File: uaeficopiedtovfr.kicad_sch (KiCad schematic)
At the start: 35 parts, among them J1 USB_B_Mini, J1 USB_C_Receptacle_USB2.0, J17 Conn_01x06, J4 1-776087-1, J5 Conn_01x05_Male, M1 Module-power_12and5V-0.2, M3 Module-knock-0.2, M3 Module-vr-discrete-0.4, M4 Module-vr-max9924-0.1, M5 Module-wbo-0.5, M6 Module:mega-mcu100/0.2, M7 Module-wbo-0.5, P1 Pad, P2 Pad, P3 Pad, P4 Pad, U4 JDY-33

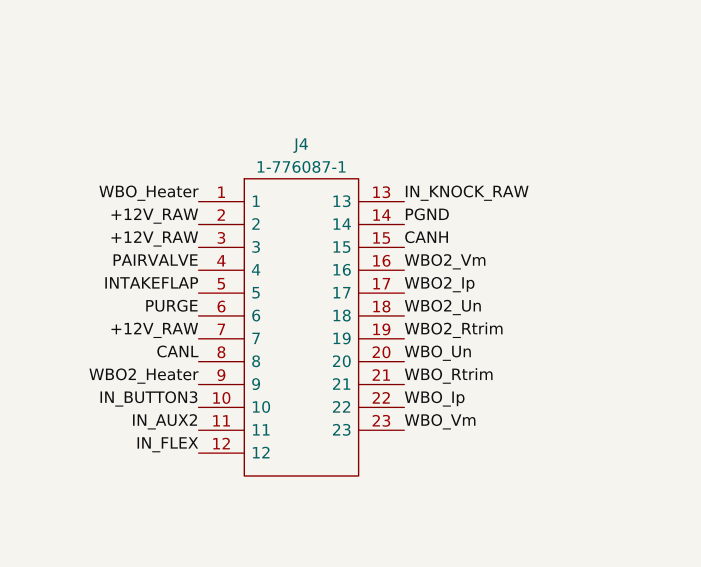
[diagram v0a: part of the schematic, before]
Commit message: swapped left and right connectors
Had the wrong idea about what was the A vs B connector, board needs routing finished
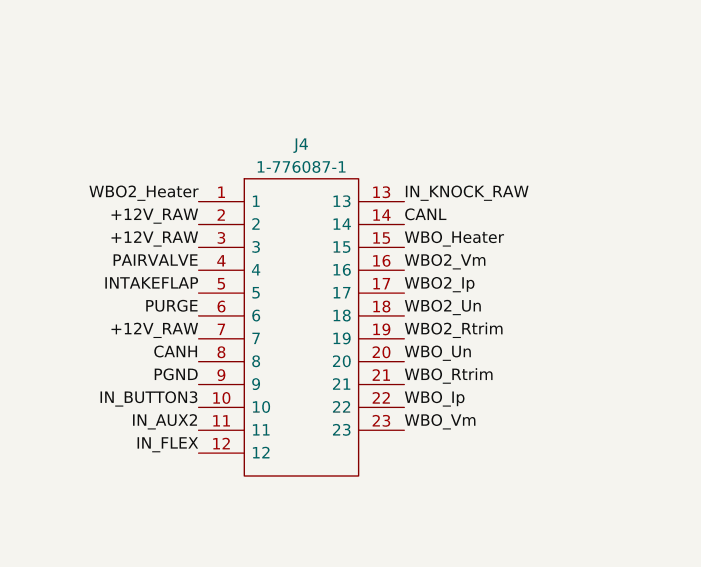
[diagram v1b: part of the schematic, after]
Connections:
- net CAN+: now also J4.8; no longer J4.15
- net CAN-: now also J4.14; no longer J4.8
- net GND: now also J4.9; no longer J4.14
- net WBO2_Heater: now also J4.1; no longer J4.9
- net WBO_Heater: now also J4.15; no longer J4.1
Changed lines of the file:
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@@
     (effects (font (size 1.27 1.27)) (justify left bottom))
   )
-  (label "PGND" (at 48.26 201.93 0) (fields_autoplaced)
-    (effects (font (size 1.27 1.27)) (justify left bottom))
+  (label "PGND" (at 25.4 219.71 180) (fields_autoplaced)
+    (effects (font (size 1.27 1.27)) (justify right bottom))
   )
   (label "CLT" (at 41.91 64.77 0) (fields_autoplaced)
@@
     (effects (font (size 1.27 1.27)) (justify right bottom))
   )
-  (label "WBO2_Heater" (at 25.4 219.71 180) (fields_autoplaced)
+  (label "WBO2_Heater" (at 25.4 199.39 180) (fields_autoplaced)
     (effects (font (size 1.27 1.27)) (justify right bottom))
   )
@@
     (effects (font (size 1.27 1.27)) (justify right bottom))
   )
-  (label "CANL" (at 25.4 217.17 180) (fields_autoplaced)
-    (effects (font (size 1.27 1.27)) (justify right bottom))
+  (label "CANL" (at 48.26 201.93 0) (fields_autoplaced)
+    (effects (font (size 1.27 1.27)) (justify left bottom))
   )
   (label "INJOUT3" (at 22.86 111.76 180) (fields_autoplaced)
@@
     (effects (font (size 1.27 1.27)) (justify left bottom))
   )
-  (label "WBO_Heater" (at 25.4 199.39 180) (fields_autoplaced)
-    (effects (font (size 1.27 1.27)) (justify right bottom))
+  (label "WBO_Heater" (at 48.26 204.47 0) (fields_autoplaced)
+    (effects (font (size 1.27 1.27)) (justify left bottom))
   )
   (label "IN_HALL1" (at 273.05 240.03 180) (fields_autoplaced)
@@
     (effects (font (size 1.27 1.27)) (justify left bottom))
   )
-  (label "CANH" (at 48.26 204.47 0) (fields_autoplaced)
-    (effects (font (size 1.27 1.27)) (justify left bottom))
+  (label "CANH" (at 25.4 217.17 180) (fields_autoplaced)
+    (effects (font (size 1.27 1.27)) (justify right bottom))
   )
   (label "WBO2_Ip" (at 195.58 -3.81 0) (fields_autoplaced)

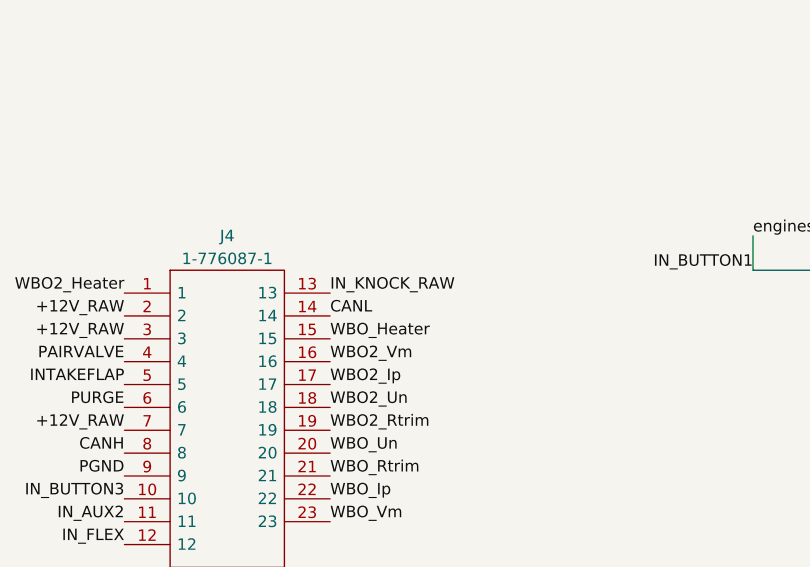
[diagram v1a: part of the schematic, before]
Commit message: Routed AUX1 input to back connector
RIP knock sensor option
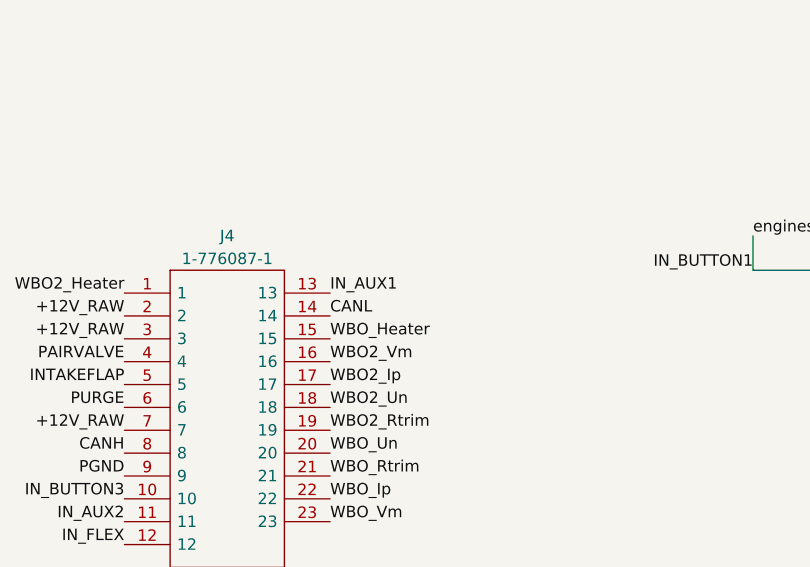
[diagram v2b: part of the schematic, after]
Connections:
- net IN_AUX1: now also J4.13
- net IN_KNOCK_RAW: no longer J4.13
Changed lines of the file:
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@@
+    (effects (font (size 1.27 1.27)) (justify left bottom))
+  )
+  (label "IN_AUX1" (at 48.26 199.39 0) (fields_autoplaced)
     (effects (font (size 1.27 1.27)) (justify left bottom))
   )
@@
     (effects (font (size 1.27 1.27)) (justify right bottom))
   )
-  (label "IN_KNOCK_RAW" (at 48.26 199.39 0) (fields_autoplaced)
-    (effects (font (size 1.27 1.27)) (justify left bottom))
-  )
   (label "OUT_INJ2" (at 124.46 119.38 180) (fields_autoplaced)

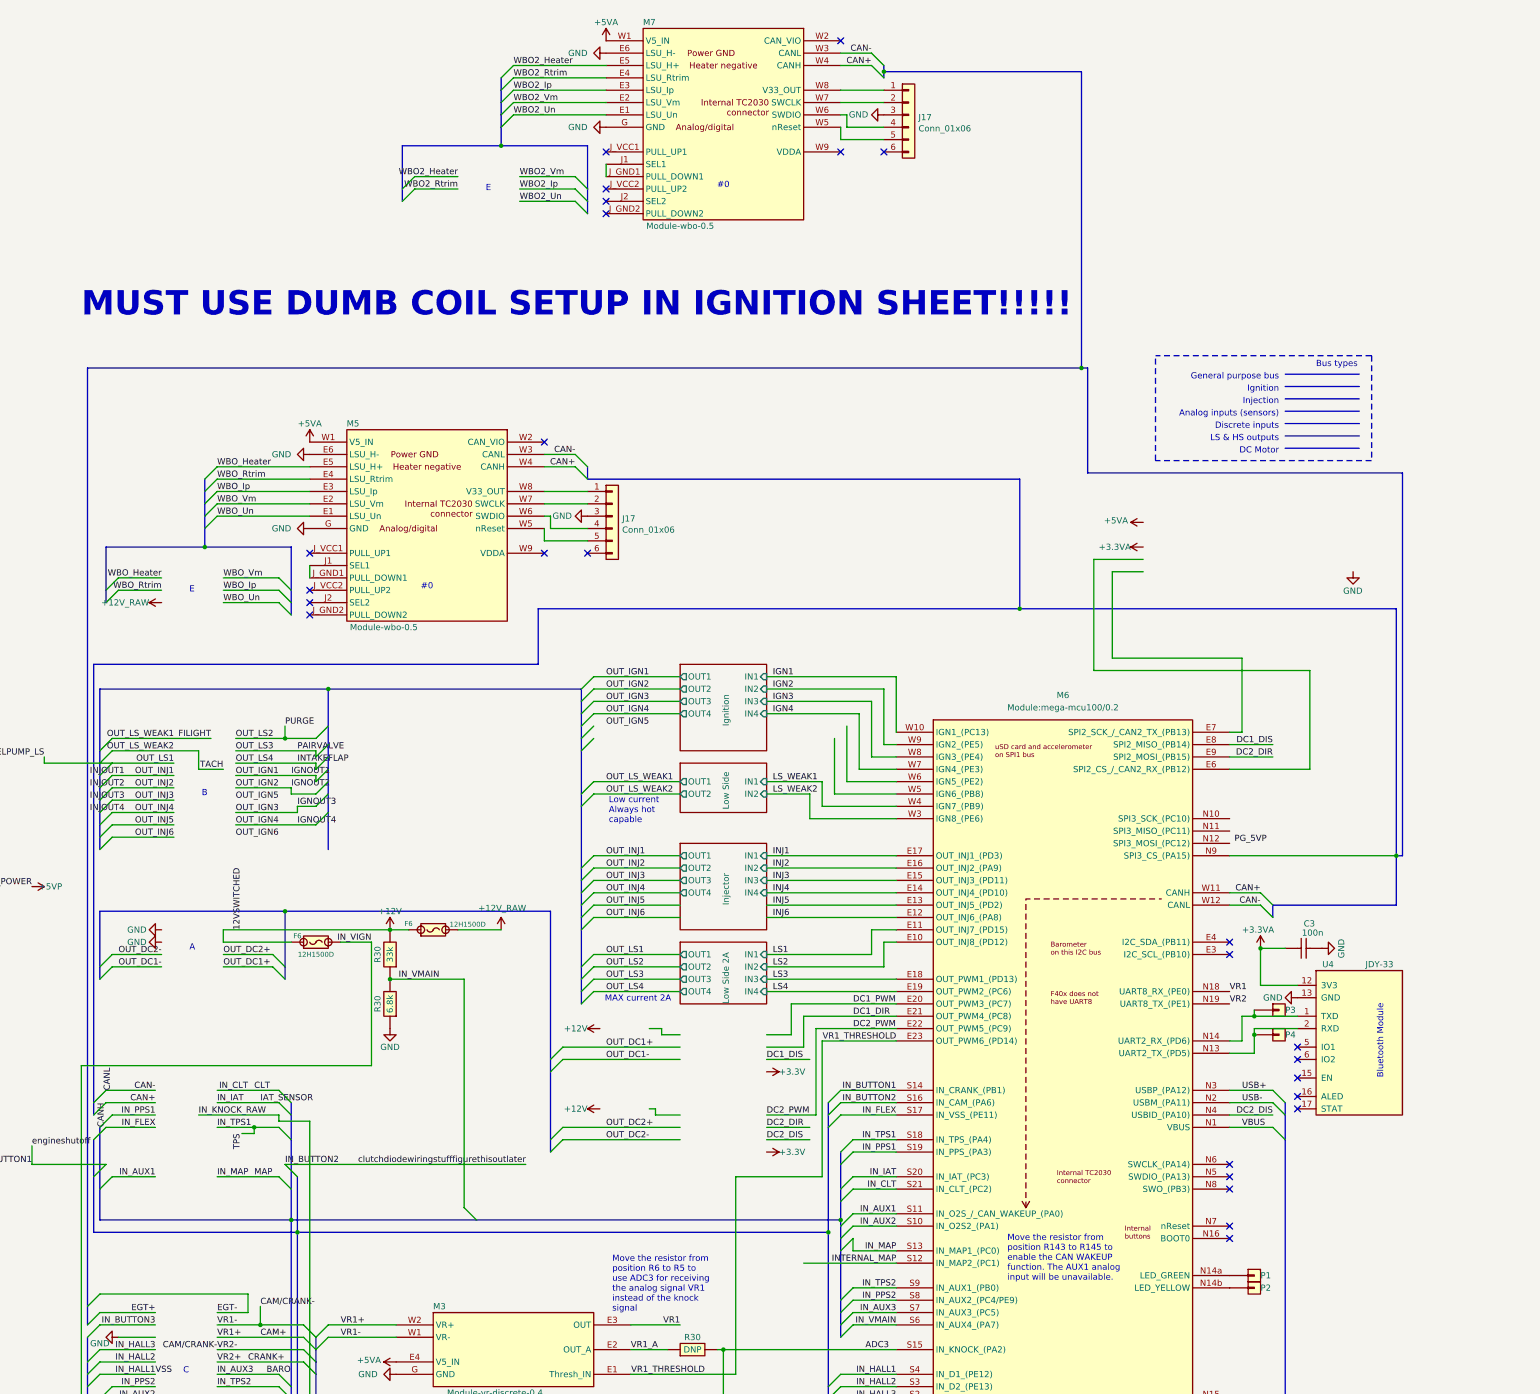
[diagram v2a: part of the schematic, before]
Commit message: Added jumpers for power to BT module and both WBO modules
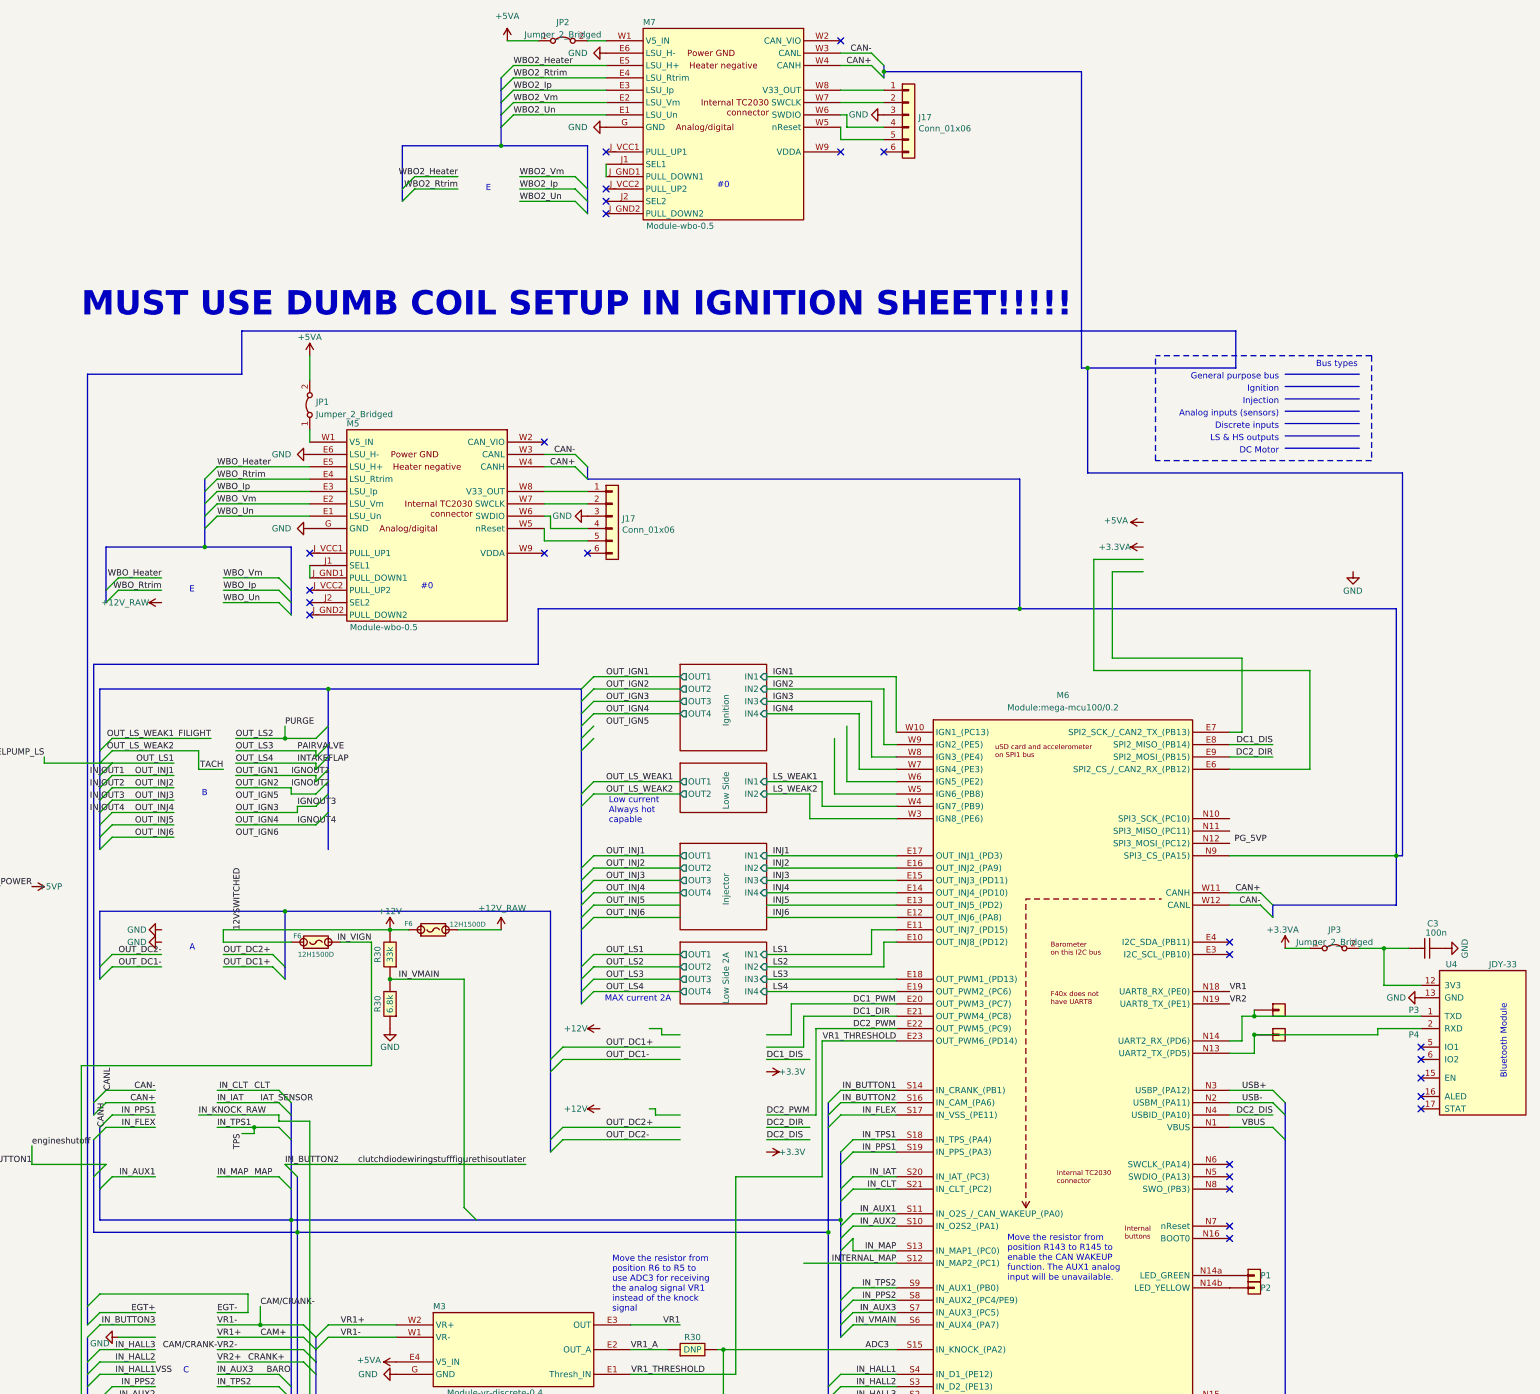
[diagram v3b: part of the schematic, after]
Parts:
- added JP1, JP2, JP3: Jumper_2_Bridged, Connector_PinHeader_2.54mm:PinHeader_1x02_P2.54mm_Vertical, symbol Jumper:Jumper_2_Bridged
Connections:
- net +3.3VA: now also JP3.1 (A); no longer C3.2, U4.12 (3V3)
- net +5VA: now also JP1.2 (B), JP2.1 (A); no longer M5.W1 (V5_IN), M7.W1 (V5_IN)
- new net: JP1.1 (A), M5.W1 (V5_IN)
- new net: C3.2, JP3.2 (B), U4.12 (3V3)
- new net: JP2.2 (B), M7.W1 (V5_IN)
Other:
- moved on the sheet: C3, U4

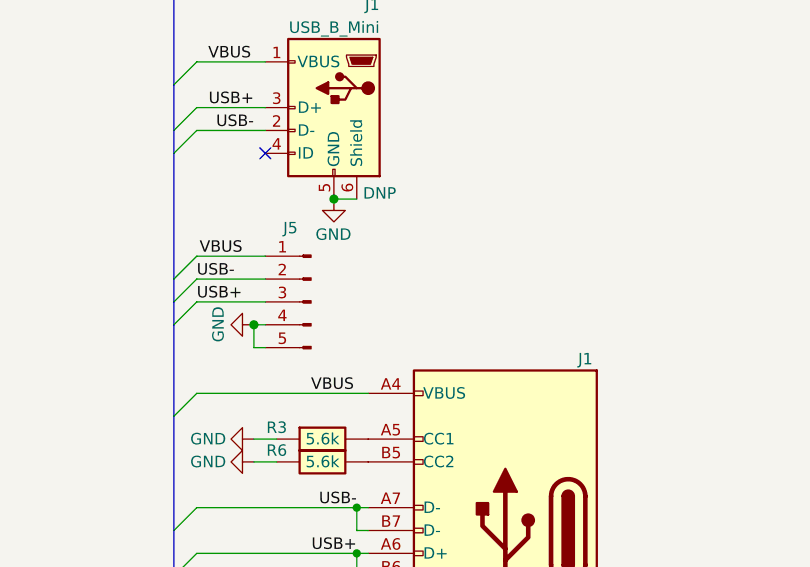
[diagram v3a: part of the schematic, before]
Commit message: fixed rear connector position, made USB more practical
Rounded off corners, changed USB connector, moved AMPSeal connector closer to board edge, changed some routing
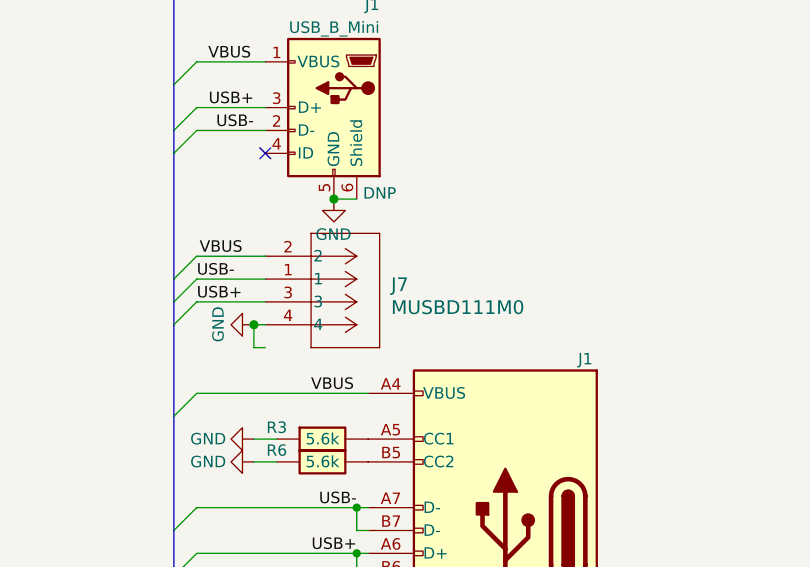
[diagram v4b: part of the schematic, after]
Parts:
- removed J5: Conn_01x05_Male, Connector_Molex:Molex_SPOX_5267-05A_1x05_P2.50mm_Vertical, symbol Connector:Conn_01x05_Pin
- added J7: MUSBD111M0, CONN4_BD111M0_AMP, symbol usbb:MUSBD111M0
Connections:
- net GND: now also J7.4
- net USB+: now also J7.3
- net USB-: now also J7.1
- net VBUS: now also J7.2
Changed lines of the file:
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@@
-    )
-  )
-  (symbol (lib_id "Connector:Conn_01x05_Pin") (at 328.93 316.23 0) (mirror y) (unit 1)
-    (in_bom yes) (on_board yes) (dnp no)
-    (property "Reference" "J5" (at 325.8313 308.0194 0)
-      (effects (font (size 1.27 1.27)) (justify right))
-    )
-    (property "Value" "Conn_01x05_Male" (at 313.1313 323.0181 0)
-      (effects (font (size 1.27 1.27)) (justify right) hide)
-    )
-    (property "Footprint" "Connector_Molex:Molex_SPOX_5267-05A_1x05_P2.50mm_Vertical" (at 328.93 316.23 0)
-      (effects (font (size 1.27 1.27)) hide)
-    )
-    (property "Datasheet" "~" (at 328.93 316.23 0)
-      (effects (font (size 1.27 1.27)) hide)
-    )
-    (pin "1")
-    (pin "2")
-    (pin "3")
-    (pin "4")
-    (pin "5")
-    (instances
-      (project "hellen125honda"
-        (path "/63d2dd9f-d5ff-4811-a88d-0ba932475460"
-          (reference "J5") (unit 1)
-        )
-      )
-      (project "uaeficopiedtovfr"
-        (path "/90b72e19-92bc-40db-bd4d-f17fb5de93ea"
-          (reference "J7") (unit 1)
-        )
-      )
-      (project "uaefi"
-        (path "/ac264c30-3e9a-4be2-b97a-9949b68bd497"
-          (reference "J7") (unit 1)
-        )
-      )
     )
   )
@@
         )
       )
+    )
+  )
+  (symbol (lib_id "usbb:MUSBD111M0") (at 323.85 311.15 0) (unit 1)
+    (in_bom yes) (on_board yes) (dnp no) (fields_autoplaced)
+    (property "Reference" "J7" (at 337.82 314.325 0)
+      (effects (font (size 1.524 1.524)) (justify left))
+    )
+    (property "Value" "MUSBD111M0" (at 337.82 316.865 0)
+      (effects (font (size 1.524 1.524)) (justify left))
+    )
+    (property "Footprint" "CONN4_BD111M0_AMP" (at 323.85 311.15 0)
+      (effects (font (size 1.27 1.27) italic) hide)
+    )
+    (property "Datasheet" "MUSBD111M0" (at 323.85 311.15 0)
+      (effects (font (size 1.27 1.27) italic) hide)
+    )
+    (pin "1")
+    (pin "2")
+    (pin "3")
+    (pin "4")
+    (instances
+      (project "uaeficopiedtovfr"
+        (path "/90b72e19-92bc-40db-bd4d-f17fb5de93ea"
+          (reference "J7") (unit 1)
+        )
+      )

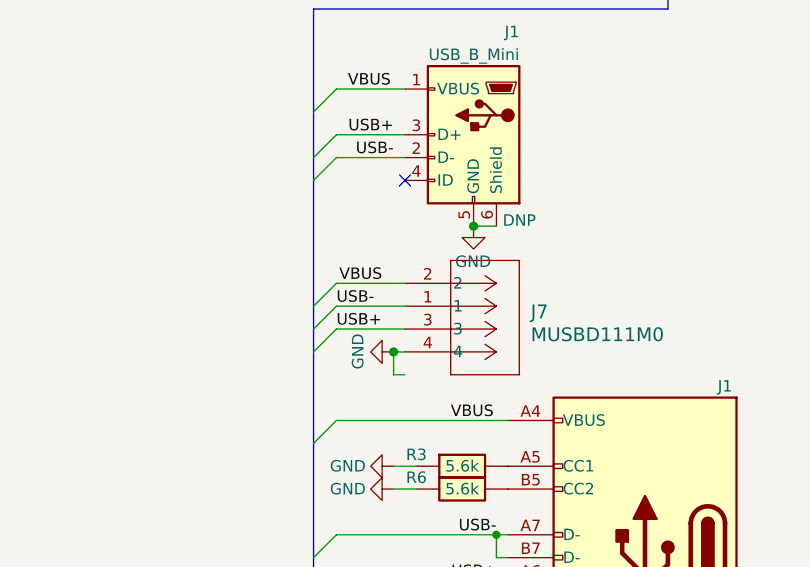
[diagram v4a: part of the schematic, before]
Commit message: touched up routing
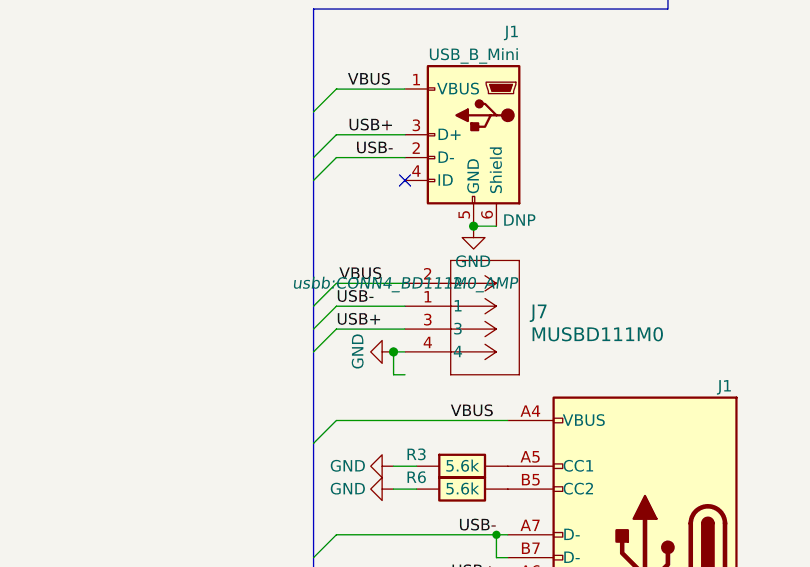
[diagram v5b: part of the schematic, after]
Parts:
- J7: footprint CONN4_BD111M0_AMP -> usbb:CONN4_BD111M0_AMP
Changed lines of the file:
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@@
       (effects (font (size 1.524 1.524)) (justify left))
     )
-    (property "Footprint" "CONN4_BD111M0_AMP" (at 323.85 311.15 0)
-      (effects (font (size 1.27 1.27) italic) hide)
+    (property "Footprint" "usbb:CONN4_BD111M0_AMP" (at 323.85 311.15 0)
+      (effects (font (size 1.27 1.27) italic))
     )
     (property "Datasheet" "MUSBD111M0" (at 323.85 311.15 0)
